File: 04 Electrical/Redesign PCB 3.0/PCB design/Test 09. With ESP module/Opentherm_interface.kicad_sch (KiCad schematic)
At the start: 20 parts, among them J2 Boiler, Q1 MMBT2907A, U3 EL357N-G, U4 EL357N-G

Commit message: Routing PCB test 9
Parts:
- U3, U4: footprint EL357N-G:OPTO_EL357N-G -> Package_SO:SOP-4_3.8x4.1mm_P2.54mm
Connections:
- net Boiler 1: now reaches D6.2 (A), D7.1 (K), J2.1 (Pin_1)
- net Boiler 2: now reaches D8.2 (A), D9.1 (K), J2.2 (Pin_2)
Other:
- moved on the sheet: J2
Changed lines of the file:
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@@
 	)
 	(junction
+		(at 66.04 87.63)
+		(diameter 0)
+		(color 0 0 0 0)
+	)
+	(junction
 		(at 128.27 105.41)
 		(diameter 0)
@@
 	)
 	(junction
+		(at 66.04 85.09)
+		(diameter 0)
+		(color 0 0 0 0)
+	)
+	(junction
 		(at 182.88 80.01)
 		(diameter 0)
@@
 	(wire
 		(pts
+			(xy 69.85 81.28) (xy 66.04 81.28)
+		)
+		(stroke
+			(width 0)
+			(type default)
+		)
+	)
+	(wire
+		(pts
 			(xy 128.27 99.06) (xy 128.27 105.41)
 		)
@@
 	(wire
 		(pts
-			(xy 87.63 85.09) (xy 97.79 85.09)
+			(xy 60.96 85.09) (xy 66.04 85.09)
+		)
+		(stroke
+			(width 0)
+			(type default)
+		)
+	)
+	(wire
+		(pts
+			(xy 66.04 85.09) (xy 97.79 85.09)
 		)
 		(stroke
@@
 	(wire
 		(pts
+			(xy 66.04 81.28) (xy 66.04 85.09)
+		)
+		(stroke
+			(width 0)
+			(type default)
+		)
+	)
+	(wire
+		(pts
+			(xy 66.04 91.44) (xy 66.04 87.63)
+		)
+		(stroke
+			(width 0)
+			(type default)
+		)
+	)
+	(wire
+		(pts
 			(xy 170.18 114.3) (xy 170.18 115.57)
 		)
@@
 	(wire
 		(pts
-			(xy 87.63 87.63) (xy 110.49 87.63)
+			(xy 60.96 87.63) (xy 66.04 87.63)
 		)
 		(stroke
@@
 	(wire
 		(pts
+			(xy 69.85 91.44) (xy 66.04 91.44)
+		)
+		(stroke
+			(width 0)
+			(type default)
+		)
+	)
+	(wire
+		(pts
 			(xy 185.42 80.01) (xy 182.88 80.01)
 		)
@@
 	(wire
 		(pts
+			(xy 66.04 87.63) (xy 110.49 87.63)
+		)
+		(stroke
+			(width 0)
+			(type default)
+		)
+	)
+	(wire
+		(pts
 			(xy 135.89 80.01) (xy 144.78 80.01)
 		)
@@
 		)
 	)
+	(global_label "Boiler 2"
+		(shape input)
+		(at 69.85 91.44 0)
+		(fields_autoplaced yes)
+		(effects
+			(font
+				(size 1.27 1.27)
+			)
+			(justify left)
+		)
+		(property "Intersheetrefs" "${INTERSHEET_REFS}"
+			(at 80.5761 91.44 0)
+			(effects
+				(font
+					(size 1.27 1.27)
+				)
+				(justify left)
+				(hide yes)
+			)
+		)
+	)
+	(global_label "Boiler 1"
+		(shape input)
+		(at 69.85 81.28 0)
+		(fields_autoplaced yes)
+		(effects
+			(font
+				(size 1.27 1.27)
+			)
+			(justify left)
+		)
+		(property "Intersheetrefs" "${INTERSHEET_REFS}"
+			(at 80.5761 81.28 0)
+			(effects
+				(font
+					(size 1.27 1.27)
+				)
+				(justify left)
+				(hide yes)
+			)
+		)
+	)
 	(global_label "boil_to_cntr"
 		(shape input)
@@
 	(symbol
 		(lib_id "Connector:Conn_01x02_Pin")
-		(at 82.55 85.09 0)
+		(at 55.88 85.09 0)
 		(unit 1)
 		(exclude_from_sim no)
@@
 		(fields_autoplaced yes)
 		(property "Reference" "J2"
-			(at 83.185 80.01 0)
+			(at 56.515 80.01 0)
 			(effects
 				(font
@@
 		)
 		(property "Value" "Boiler"
-			(at 83.185 82.55 0)
+			(at 56.515 82.55 0)
 			(effects
 				(font
@@
 		)
 		(property "Footprint" "Connector_JST:JST_SH_SM02B-SRSS-TB_1x02-1MP_P1.00mm_Horizontal"
-			(at 82.55 85.09 0)
+			(at 55.88 85.09 0)
 			(effects
 				(font
@@
 		)
 		(property "Datasheet" "https://www.lcsc.com/datasheet/lcsc_datasheet_2304140030_JST-SM02B-SRSS-TB-LF-SN_C160402.pdf"
-			(at 82.55 85.09 0)
+			(at 55.88 85.09 0)
 			(effects
 				(font
@@
 		)
 		(property "Description" "Generic connector, single row, 01x02, script generated"
-			(at 82.55 85.09 0)
+			(at 55.88 85.09 0)
 			(effects
 				(font
@@
 		)
 		(property "Field5" ""
-			(at 82.55 85.09 0)
+			(at 55.88 85.09 0)
 			(effects
 				(font
@@
 		)
 		(property "LCSC Part # " "C160402"
-			(at 82.55 85.09 0)
+			(at 55.88 85.09 0)
 			(effects
 				(font
@@
 			)
 		)
-		(property "Footprint" "EL357N-G:OPTO_EL357N-G"
+		(property "Footprint" "Package_SO:SOP-4_3.8x4.1mm_P2.54mm"
 			(at 168.91 82.55 0)
 			(effects
@@
 			)
 		)
-		(property "Footprint" "EL357N-G:OPTO_EL357N-G"
+		(property "Footprint" "Package_SO:SOP-4_3.8x4.1mm_P2.54mm"
 			(at 182.88 107.95 0)
 			(effects

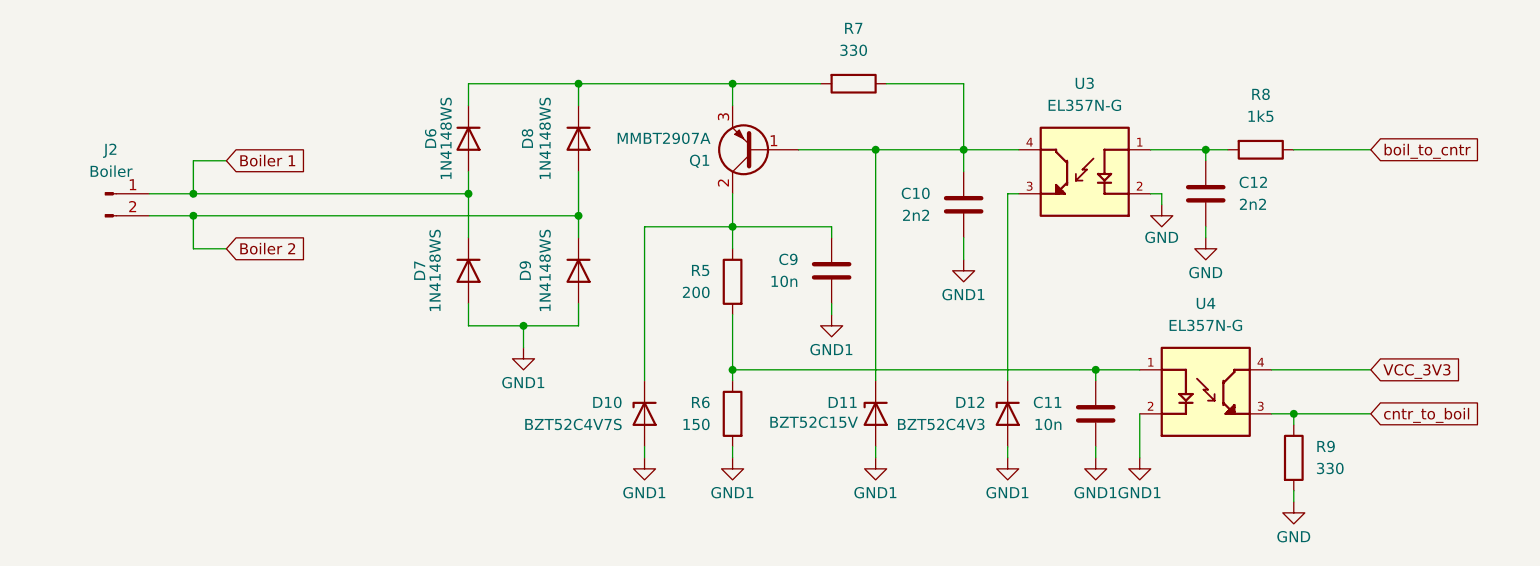
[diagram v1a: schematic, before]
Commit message: Logo added to PCB
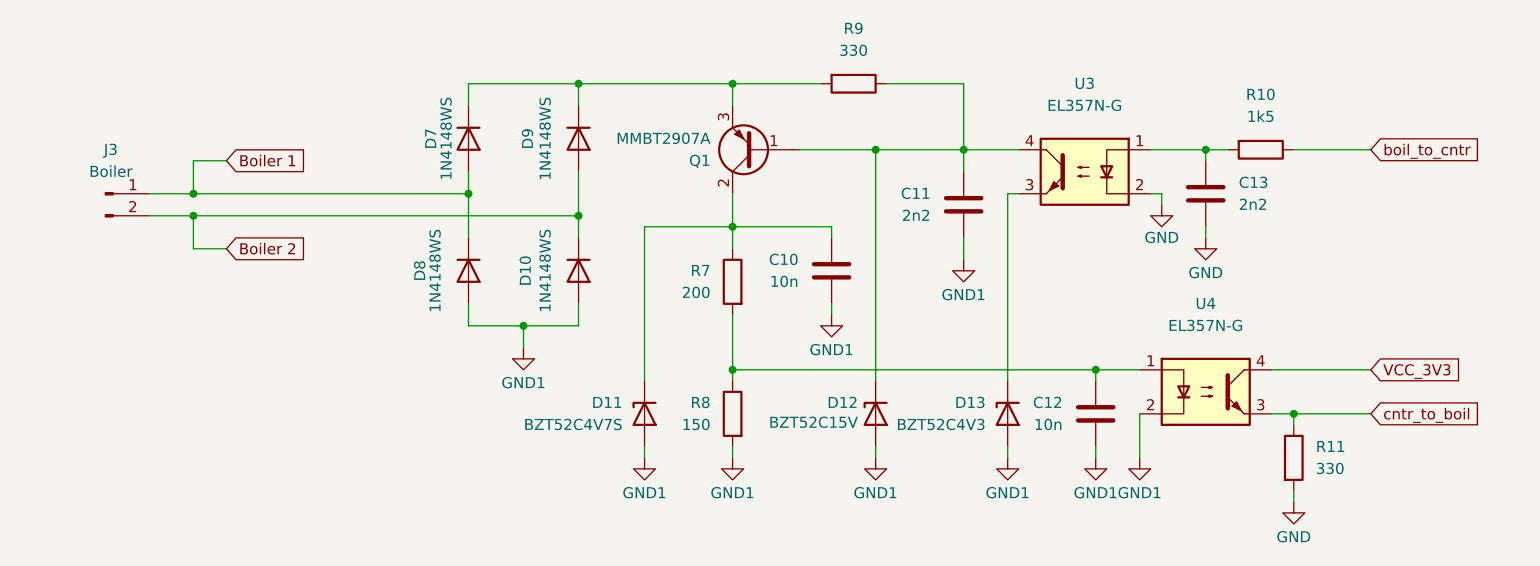
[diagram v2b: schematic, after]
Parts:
- U3, U4: footprint Package_SO:SOP-4_3.8x4.1mm_P2.54mm -> Package_SO:SO-4_4.4x3.6mm_P2.54mm; symbol EL357N-G:EL357N-G -> Isolator:LTV-357T
- renumbered C9 to C10, C10 to C11, C11 to C12, C12 to C13, D9 to D10, D10 to D11, D11 to D12, D12 to D13, D6 to D7, D7 to D8, D8 to D9, J2 to J3, R8 to R10, R9 to R11, R5 to R7, R6 to R8, R7 to R9

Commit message: As ordered at JLCPCB
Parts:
- removed C10, C12: 10n, Capacitor_SMD:C_0603_1608Metric, symbol Device:C
- removed C11, C13: 2n2, Capacitor_SMD:C_0603_1608Metric, symbol Device:C
- removed J3: Boiler, Connector_JST:JST_SH_SM02B-SRSS-TB_1x02-1MP_P1.00mm_Horizontal, symbol Connector:Conn_01x02_Pin
- added J2: Boiler, Connector_JST:JST_SH_SM02B-SRSS-TB_1x02-1MP_P1.00mm_Horizontal, symbol Connector_Generic_Shielded:Conn_01x02_Shielded
- R11: footprint Diode_SMD:D_0805_2012Metric -> Resistor_SMD:R_0805_2012Metric
- R7: value 200 -> 180; LCSC Part #  C25292 -> C25270
- R8: value 150 -> 100; LCSC Part #  C17471 -> C17408
- U3, U4: Availability In Stock -> (none); Check_prices https://www.snapeda.com/parts/EL357N-G/Everlight+Electronic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 -> (none); Description_1 Optoisolator Transistor Output 3750Vrms 1 Channel 4-SOP (2.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 -> (none); MANUFACTURER Everlight -> (none); MAXIMUM_PACKAGE_HEIGHT 2.00mm -> (none); MF Everlight Electronics -> (none); MP EL357N-G -> (none); PARTREV 6 -> (none); Package SOP-4 Everlight -> (none); Price None -> (none); STANDARD Manufacturer Recommendations -> (none); SnapEDA_Link https://www.snapeda.com/parts/EL357N-G/Everlight+Electronic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 -> (none)
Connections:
- net Boiler 1: now also J2.1 (Pin_1)
- net Boiler 2: now also J2.2 (Pin_2)
- net GND1: now also J2.MP (Shield)
- net boiler: now reaches R7.2, R8.1, U4.1
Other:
- moved on the sheet: R10, R11, R9
